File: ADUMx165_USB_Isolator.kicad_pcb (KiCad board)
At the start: 4 copper layers, 50 x 36.5 mm, 60 parts, among them J1 XKB_U262-16XN-4BVC11, J2 HRO_TYPE-C-31-M-17, J3 XKB_U221-041N-4V33, J4 XKB_U221-041N-4V33, J5 XKB_U221-041N-4V33, J6 XKB_U221-041N-4V33, T1 DA2303-AL, U1 SN6505BDBV, U10 USBLC6-2P6, U2 USBLC6-2P6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

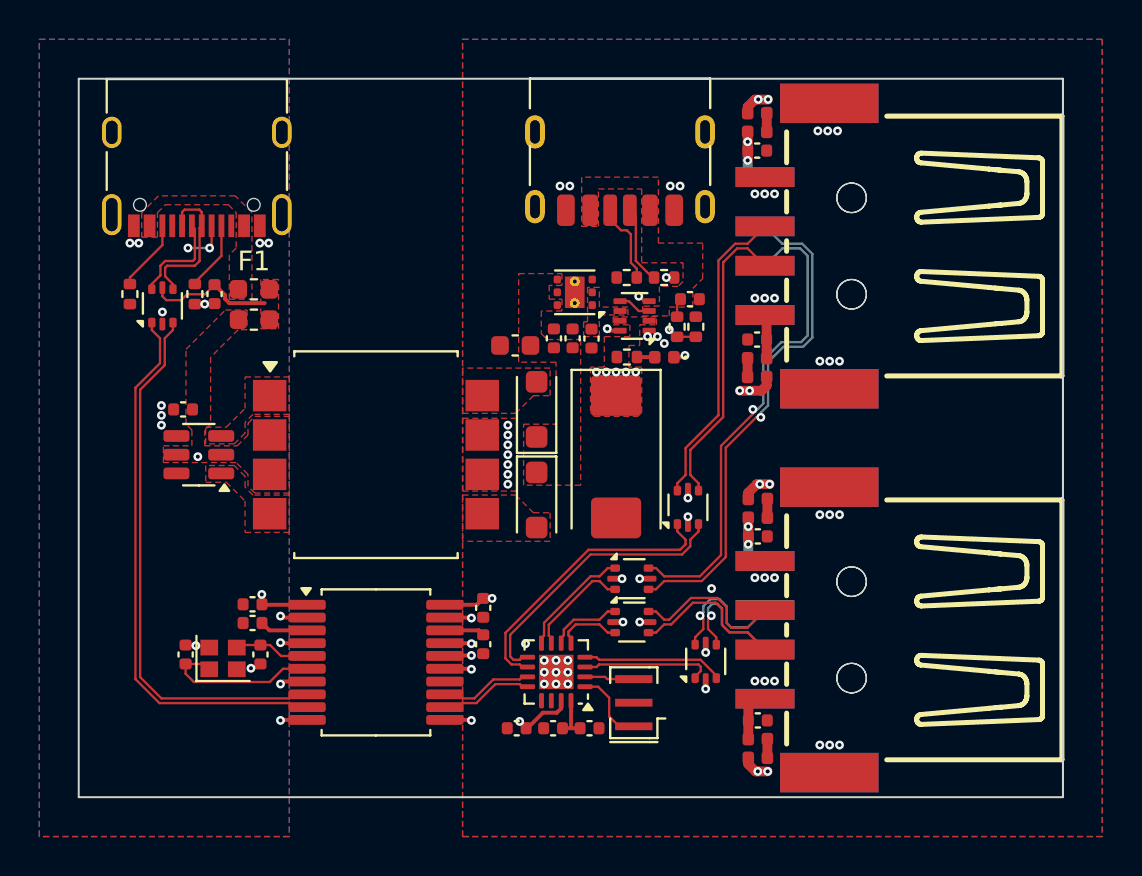
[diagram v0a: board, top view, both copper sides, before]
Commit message: Update workflow Embed 3D models Board shape & silkscreen change
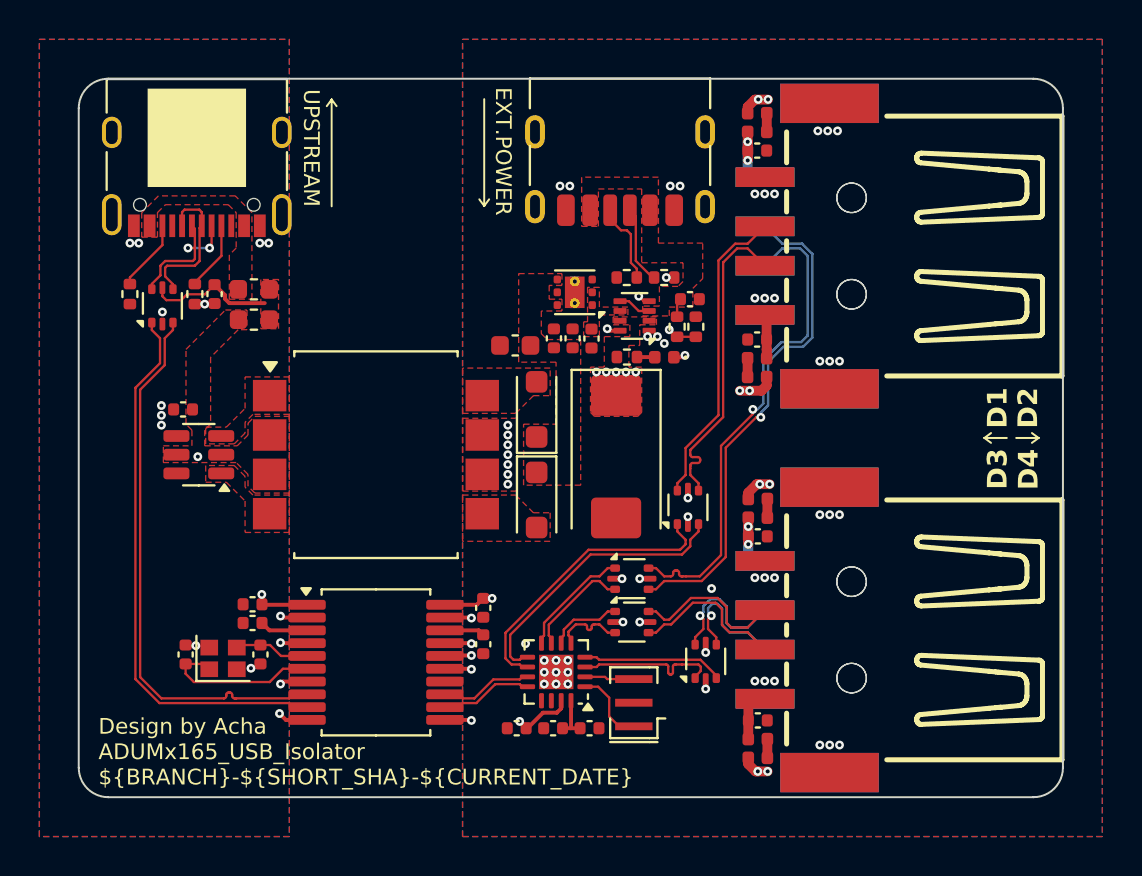
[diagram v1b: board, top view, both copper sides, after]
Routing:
- net /D4-: track 6.60 -> 7.44 mm
- net /D1A-: track 15.2 -> 16.0 mm
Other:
- outline, holes or cut-outs redrawn
- board text added: "0.1200 mm / 0.1200 mm"
- board text added: "0.2000 mm"
- board text added: "1.6000 mm"
- board text added: "4"
- board text added: "50.0000 mm x 36.5000 mm"
- board text added: "BOARD CHARACTERISTICS"
- board text added: "D1"
- board text added: "D2"
- board text added: "D3"
- board text added: "D4"
- board text added: "Design by Acha ADUMx165_USB_Isolator ${BRANCH}-${SHORT_SHA}-${CURRENT_DATE}"
- board text added: "EXT.POWER"
- board text added: "Not specified"
- board text added: "UPSTREAM"
- board text added: "否"
- board text added: "存在半孔焊盘:"
- board text added: "是"
- board text added: "最小孔径:"
- board text added: "最小走线/间距:"
- board text added: "板厚:"
- board text added: "板子整体尺寸:"
- board text added: "板边倒角处理:"
- board text added: "铜层数量:"
- board text added: "镀铜处理:"
- board text added: "阻抗控制:"
- board text added: "需要电镀板边:"

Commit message: Delete notes in PCB file Update workflow
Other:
- board text removed: "0.1200 mm / 0.1200 mm"
- board text removed: "0.2000 mm"
- board text removed: "1.6000 mm"
- board text removed: "4"
- board text removed: "50.0000 mm x 36.5000 mm"
- board text removed: "BOARD CHARACTERISTICS"
- board text removed: "Not specified"
- board text removed: "否"
- board text removed: "存在半孔焊盘:"
- board text removed: "是"
- board text removed: "最小孔径:"
- board text removed: "最小走线/间距:"
- board text removed: "板厚:"
- board text removed: "板子整体尺寸:"
- board text removed: "板边倒角处理:"
- board text removed: "铜层数量:"
- board text removed: "镀铜处理:"
- board text removed: "阻抗控制:"
- board text removed: "需要电镀板边:"

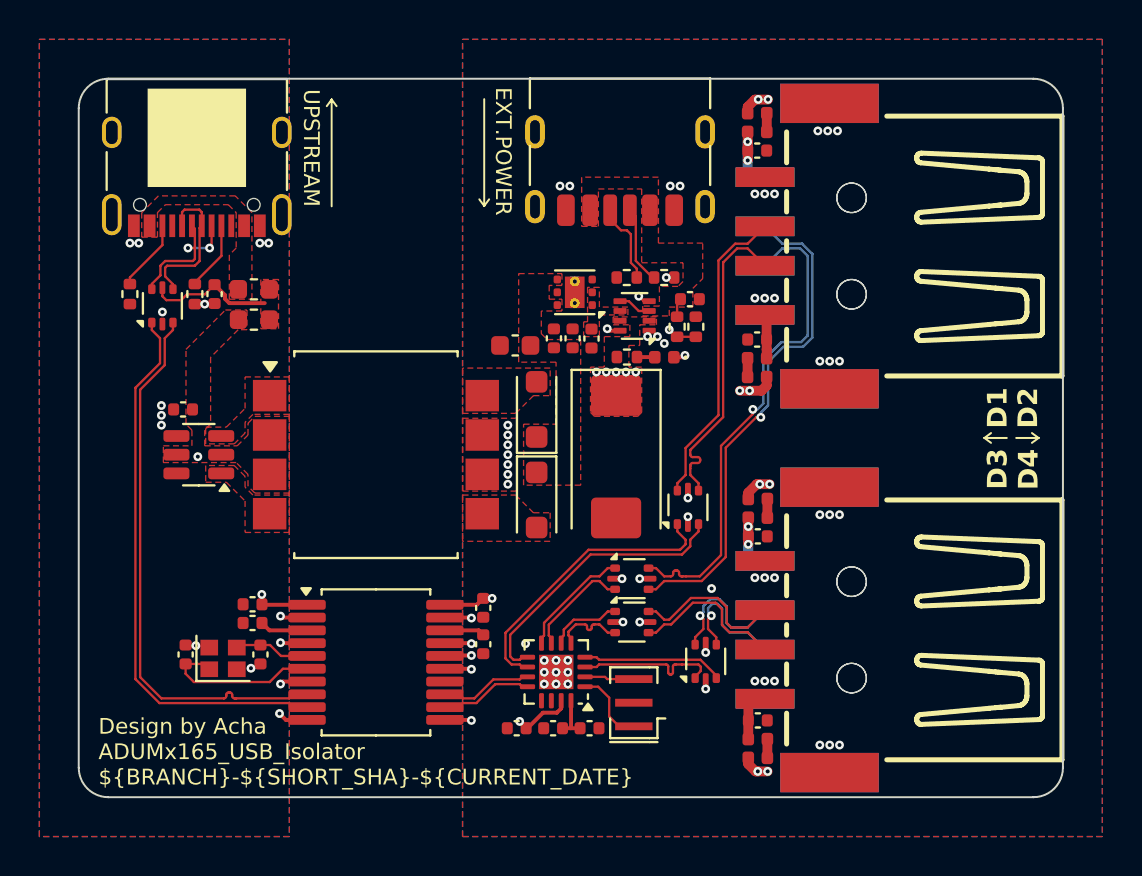
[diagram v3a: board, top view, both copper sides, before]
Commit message: Add GND Vias Update Workflow
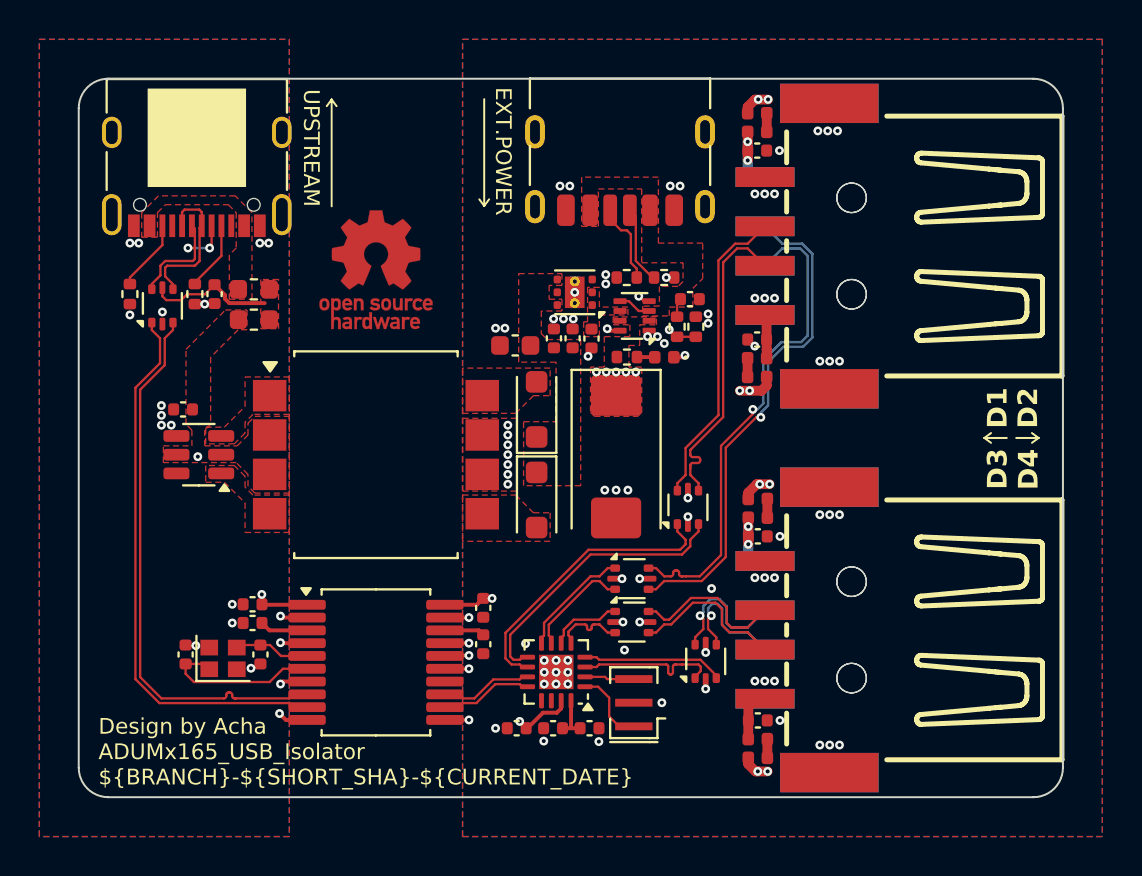
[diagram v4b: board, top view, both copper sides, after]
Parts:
- added REF**: OSHW-Logo_5.7x6mm_Copper, Symbol:OSHW-Logo_5.7x6mm_Copper, F.Cu at (125.1, 109.2)
- added REF**: OSHW-Logo_5.7x6mm_Copper, , F.Cu at (125.1, 109.2)
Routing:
- net GND2: track 8.59 -> 7.93 mm, vias 59 -> 82
- net GND1: vias 15 -> 19
